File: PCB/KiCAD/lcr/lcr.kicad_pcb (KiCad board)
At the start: 4 copper layers, 100 x 100 mm, 160 parts, among them J1 Conn_Coaxial, J2 Conn_Coaxial, J3 Conn_Coaxial, J4 Conn_Coaxial, J6 Screw_Terminal_01x02, J7 Barrel_Jack_Switch, J8 Conn_01x09_Pin, J9 Conn_01x14_Pin, U1 OPA2365AIDR, U10 MC7805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

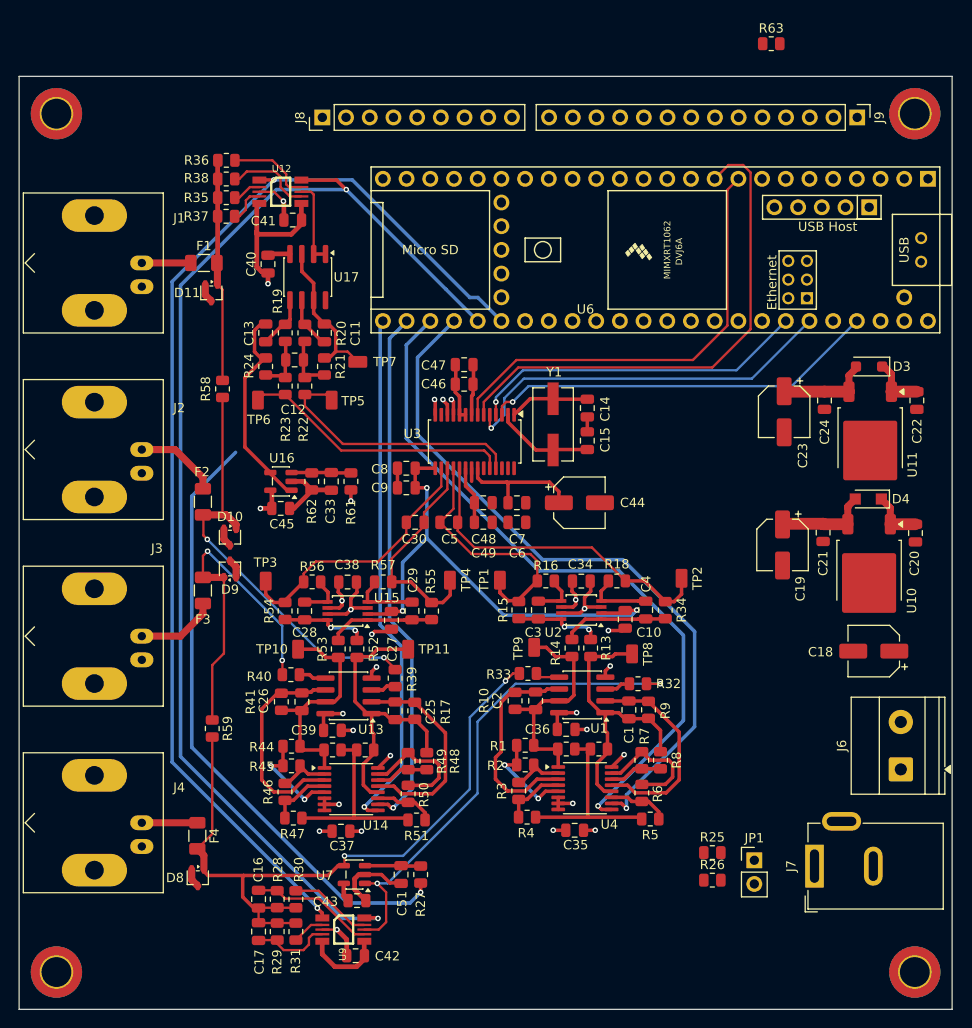
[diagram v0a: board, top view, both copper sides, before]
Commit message: top level pcb routing
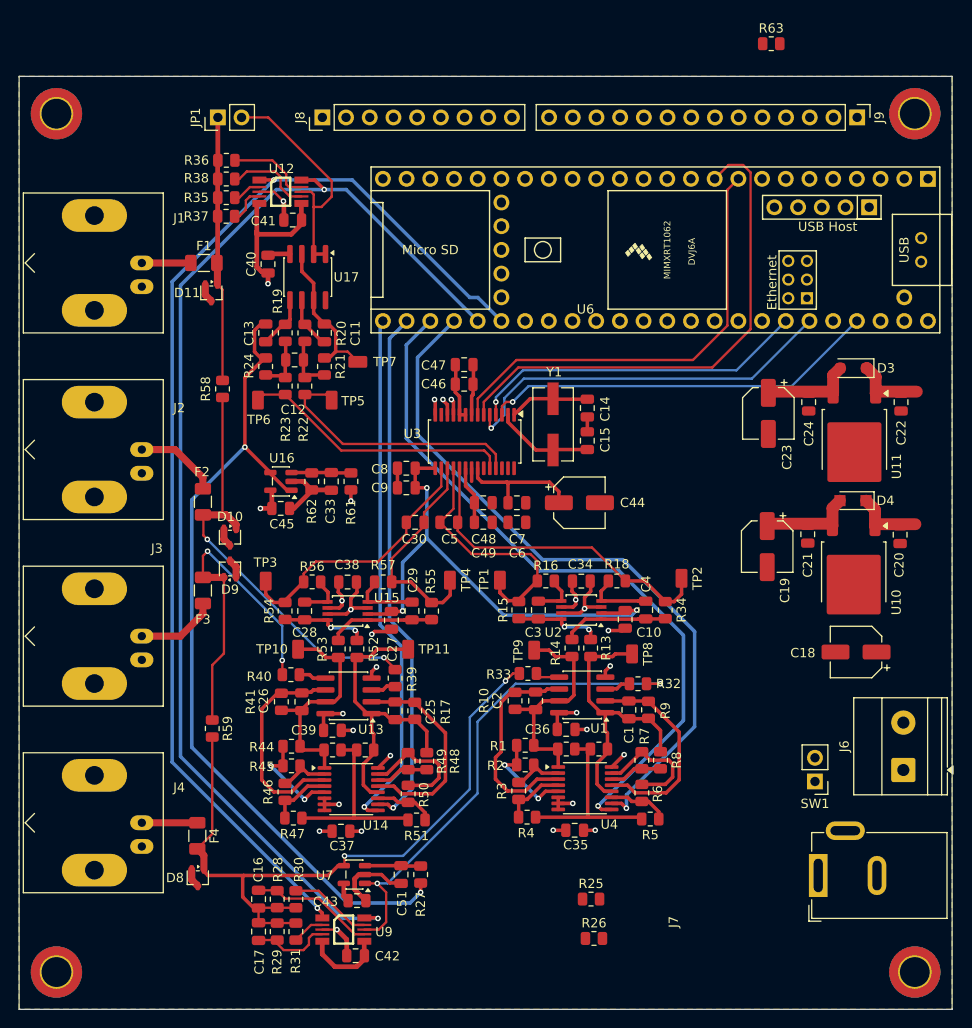
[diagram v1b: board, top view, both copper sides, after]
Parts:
- added SW1: SW_SPST, Connector_PinHeader_2.54mm:PinHeader_1x02_P2.54mm_Vertical, F.Cu at (185.3, 125.6)
- moved JP1 98.2 mm to (121.3, 54.4), turned to 90 degrees
- moved R26 14.1 mm to (161.6, 142.4)
- moved R25 13.9 mm to (161.3, 138.2)
- moved C18 1.90 mm to (189.7, 111.7)
- moved C22 1.70 mm to (194.5, 84.9)
- moved C24 1.70 mm to (184.6, 84.9)
- moved D3 1.70 mm to (189.4, 81.3)
- moved C23 1.70 mm to (180.3, 86.1)
- moved U11 1.70 mm to (189.5, 89.0)
- moved D4 1.65 mm to (189.4, 95.5)
- moved C19 1.65 mm to (180.2, 100.4)
- moved C20 1.65 mm to (194.4, 99.1)
- moved C21 1.65 mm to (184.5, 99.1)
- moved U10 1.65 mm to (189.5, 103.2)
- moved J7 1.08 mm to (185.7, 135.7)
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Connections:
- J6 pad 1: Net-(J6-Pin_1) -> GND
- J6 pad 2: GND -> Net-(J6-Pin_2)
- J7 pad 1: Net-(J6-Pin_1) -> Net-(J6-Pin_2)
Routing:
- net /sig_buf: track 9.14 -> 25.7 mm
- net /sig_conn: track 24.0 -> 28.6 mm
- net +12V: track 11.7 -> 15.2 mm
- net RSEL_1: track 127.5 -> 125.2 mm
- net VMID: track 89.2 -> 90.2 mm, vias 1 -> 2
- added copper zone on In2.Cu, net +5VA
- added copper zone on F.Cu, net GND
